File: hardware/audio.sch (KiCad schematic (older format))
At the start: 29 parts, among them U12 HX9193-33GB, U4 FM8002A, U5 TM8211, U6 FM8002A

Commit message: Finished routing rev5
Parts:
- R30: value 10 -> dnp
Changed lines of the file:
@@
 P 2550 3700
 F 0 "R30" V 2343 3700 50  0000 C CNN
-F 1 "10" V 2434 3700 50  0000 C CNN
+F 1 "dnp" V 2434 3700 50  0000 C CNN
 F 2 "Resistor_SMD:R_0603_1608Metric" V 2480 3700 50  0001 C CNN
 F 3 "~" H 2550 3700 50  0001 C CNN

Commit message: Fixed BOM lines
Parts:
- R28: LCSC (none) -> C22859
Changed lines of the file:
@@
 F 2 "Resistor_SMD:R_0603_1608Metric" V 2330 3700 50  0001 C CNN
 F 3 "~" H 2400 3700 50  0001 C CNN
-F 4 "" H 2400 3700 50  0001 C CNN "LCSC"
+F 4 "C22859" H 2400 3700 50  0001 C CNN "LCSC"
 	1    2400 3700
 	1    0    0    1

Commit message: Value cleanup
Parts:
- C26, C27: dnp (none) -> y
- R13, R15, R19, R20: value 5K1 -> 5k1
- R16, R18, R21, R22: value 10K -> 10k
- U12: value HX9193-33GB -> HX9193-33GB; dnp (none) -> y
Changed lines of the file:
@@
 P 5050 3050
 F 0 "R18" V 4843 3050 50  0000 C CNN
-F 1 "10K" V 4934 3050 50  0000 C CNN
+F 1 "10k" V 4934 3050 50  0000 C CNN
 F 2 "Resistor_SMD:R_0603_1608Metric" V 4980 3050 50  0001 C CNN
 F 3 "~" H 5050 3050 50  0001 C CNN
@@
 P 4750 3050
 F 0 "R16" V 4543 3050 50  0000 C CNN
-F 1 "10K" V 4634 3050 50  0000 C CNN
+F 1 "10k" V 4634 3050 50  0000 C CNN
 F 2 "Resistor_SMD:R_0603_1608Metric" V 4680 3050 50  0001 C CNN
 F 3 "~" H 4750 3050 50  0001 C CNN
@@
 P 4000 3050
 F 0 "R15" V 3793 3050 50  0000 C CNN
-F 1 "5K1" V 3884 3050 50  0000 C CNN
+F 1 "5k1" V 3884 3050 50  0000 C CNN
 F 2 "Resistor_SMD:R_0603_1608Metric" V 3930 3050 50  0001 C CNN
 F 3 "~" H 4000 3050 50  0001 C CNN
@@
 P 3700 3050
 F 0 "R13" V 3493 3050 50  0000 C CNN
-F 1 "5K1" V 3584 3050 50  0000 C CNN
+F 1 "5k1" V 3584 3050 50  0000 C CNN
 F 2 "Resistor_SMD:R_0603_1608Metric" V 3630 3050 50  0001 C CNN
 F 3 "~" H 3700 3050 50  0001 C CNN
@@
 P 5050 3450
 F 0 "R22" V 4843 3450 50  0000 C CNN
-F 1 "10K" V 4934 3450 50  0000 C CNN
+F 1 "10k" V 4934 3450 50  0000 C CNN
 F 2 "Resistor_SMD:R_0603_1608Metric" V 4980 3450 50  0001 C CNN
 F 3 "~" H 5050 3450 50  0001 C CNN
@@
 P 4750 3450
 F 0 "R21" V 4543 3450 50  0000 C CNN
-F 1 "10K" V 4634 3450 50  0000 C CNN
+F 1 "10k" V 4634 3450 50  0000 C CNN
 F 2 "Resistor_SMD:R_0603_1608Metric" V 4680 3450 50  0001 C CNN
 F 3 "~" H 4750 3450 50  0001 C CNN
@@
 P 4000 3450
 F 0 "R20" V 3793 3450 50  0000 C CNN
-F 1 "5K1" V 3884 3450 50  0000 C CNN
+F 1 "5k1" V 3884 3450 50  0000 C CNN
 F 2 "Resistor_SMD:R_0603_1608Metric" V 3930 3450 50  0001 C CNN
 F 3 "~" H 4000 3450 50  0001 C CNN
@@
 P 3700 3450
 F 0 "R19" V 3493 3450 50  0000 C CNN
-F 1 "5K1" V 3584 3450 50  0000 C CNN
+F 1 "5k1" V 3584 3450 50  0000 C CNN
 F 2 "Resistor_SMD:R_0603_1608Metric" V 3630 3450 50  0001 C CNN
 F 3 "~" H 3700 3450 50  0001 C CNN
@@
 F 3 "~" H 1100 4400 50  0001 C CNN
 F 4 "C15849" H 1100 4400 50  0001 C CNN "LCSC"
+F 5 "y" V 1100 4400 50  0001 C CNN "dnp"
 	1    1100 4400
 	0    -1   1    0
@@
 F 3 "~" H 2200 4400 50  0001 C CNN
 F 4 "C15849" H 2200 4400 50  0001 C CNN "LCSC"
+F 5 "y" V 2200 4400 50  0001 C CNN "dnp"
 	1    2200 4400
 	0    -1   1    0
@@
 AR Path="/5DD7D9A9/5EE458C0" Ref="U12"  Part="1"
 F 0 "U12" H 1650 5067 50  0000 C CNN
-F 1 " HX9193-33GB" H 1650 4976 50  0000 C CNN
+F 1 "HX9193-33GB" H 1650 4976 50  0000 C CNN
 F 2 "Package_TO_SOT_SMD:SOT-23-5" H 1650 4300 50  0001 C CNN
 F 3 "" H 1400 4950 50  0001 C CNN
 F 4 "C296123" H 1650 4700 50  0001 C CNN "LCSC"
+F 5 "y" H 1650 4700 50  0001 C CNN "dnp"
 	1    1650 4700
 	1    0    0    -1

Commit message: Few more dnp
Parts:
- R30: dnp (none) -> y
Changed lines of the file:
@@
 F 3 "~" H 2550 3700 50  0001 C CNN
 F 4 "" H 2550 3700 50  0001 C CNN "LCSC"
+F 5 "y" H 2550 3700 50  0001 C CNN "dnp"
 	1    2550 3700
 	1    0    0    1

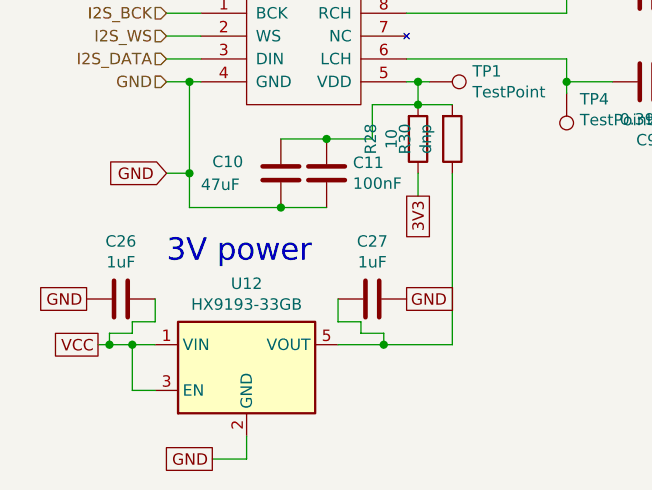
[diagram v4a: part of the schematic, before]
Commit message: Added testpoints to audio lines
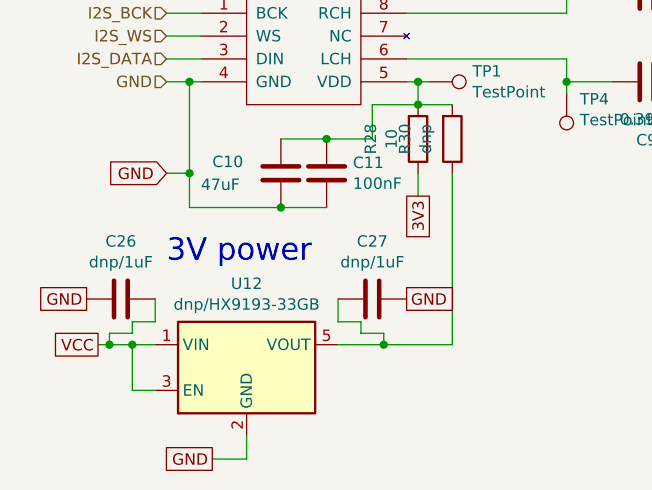
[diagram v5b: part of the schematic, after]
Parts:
- C26, C27: value 1uF -> dnp/1uF; LCSC C15849 -> (none)
- U12: value HX9193-33GB -> dnp/HX9193-33GB; LCSC C296123 -> (none)
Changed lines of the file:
@@
 AR Path="/5DD7D9A9/5EE458A4" Ref="C26"  Part="1"
 F 0 "C26" V 848 4400 50  0000 C CNN
-F 1 "1uF" V 939 4400 50  0000 C CNN
+F 1 "dnp/1uF" V 939 4400 50  0000 C CNN
 F 2 "Capacitor_SMD:C_0603_1608Metric" H 1138 4250 50  0001 C CNN
 F 3 "~" H 1100 4400 50  0001 C CNN
-F 4 "C15849" H 1100 4400 50  0001 C CNN "LCSC"
+F 4 "" H 1100 4400 50  0001 C CNN "LCSC"
 F 5 "y" V 1100 4400 50  0001 C CNN "dnp"
 	1    1100 4400
@@
 AR Path="/5DD7D9A9/5EE458AB" Ref="C27"  Part="1"
 F 0 "C27" V 1948 4400 50  0000 C CNN
-F 1 "1uF" V 2039 4400 50  0000 C CNN
+F 1 "dnp/1uF" V 2039 4400 50  0000 C CNN
 F 2 "Capacitor_SMD:C_0603_1608Metric" H 2238 4250 50  0001 C CNN
 F 3 "~" H 2200 4400 50  0001 C CNN
-F 4 "C15849" H 2200 4400 50  0001 C CNN "LCSC"
+F 4 "" H 2200 4400 50  0001 C CNN "LCSC"
 F 5 "y" V 2200 4400 50  0001 C CNN "dnp"
 	1    2200 4400
@@
 AR Path="/5DD7D9A9/5EE458C0" Ref="U12"  Part="1"
 F 0 "U12" H 1650 5067 50  0000 C CNN
-F 1 "HX9193-33GB" H 1650 4976 50  0000 C CNN
+F 1 "dnp/HX9193-33GB" H 1650 4976 50  0000 C CNN
 F 2 "Package_TO_SOT_SMD:SOT-23-5" H 1650 4300 50  0001 C CNN
 F 3 "" H 1400 4950 50  0001 C CNN
-F 4 "C296123" H 1650 4700 50  0001 C CNN "LCSC"
+F 4 "" H 1650 4700 50  0001 C CNN "LCSC"
 F 5 "y" H 1650 4700 50  0001 C CNN "dnp"
 	1    1650 4700
